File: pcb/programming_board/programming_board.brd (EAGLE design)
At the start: 57.9 x 35.5 mm, 34 parts

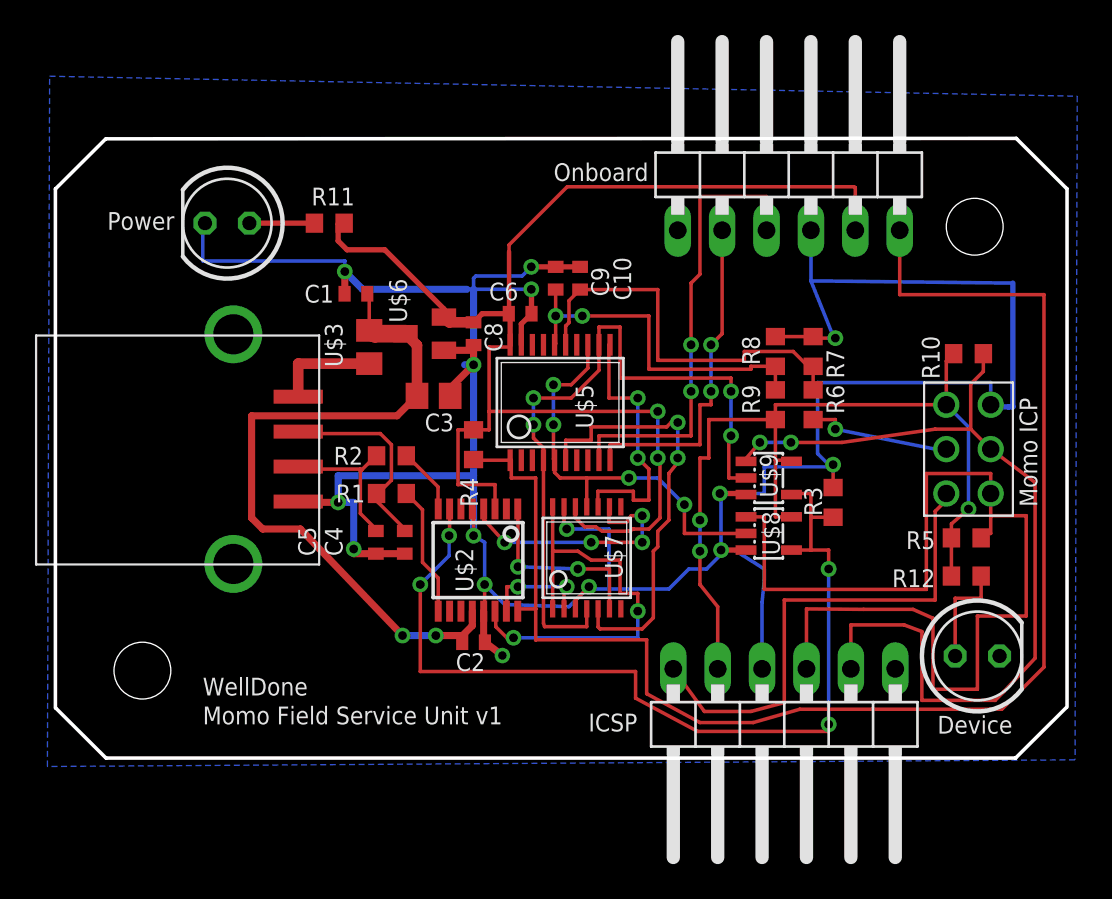
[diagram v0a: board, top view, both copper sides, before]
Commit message: Updated MoMo FSU to version 2.  Following major changes: 1. Removed unneeded header for momo programming. 2. Removed mux and analog switches allowing serial passthrough, all communication with momo will be over mib. 3. standardized momo connector 4. relaid out board
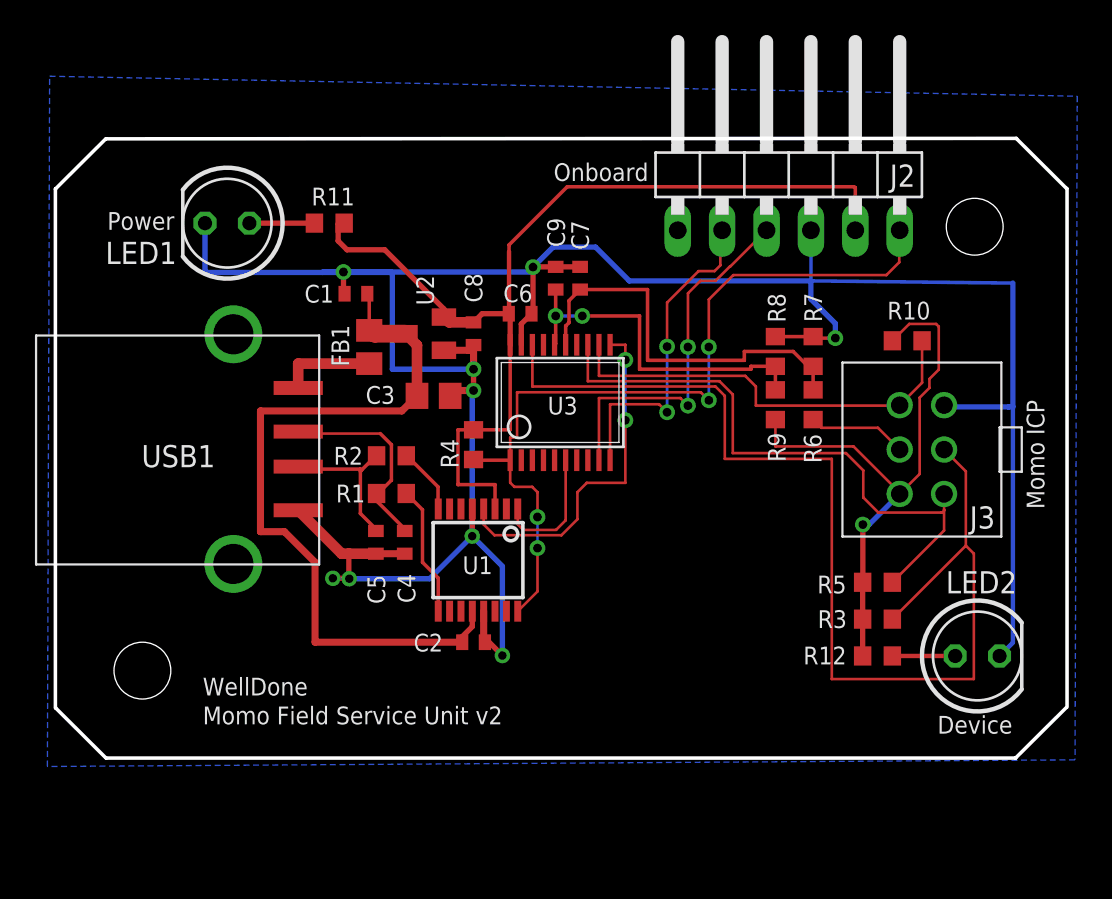
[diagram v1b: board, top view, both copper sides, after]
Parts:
- removed MOMO-ICSP: (no value), pinhead:1X06/90
- removed U$4: 2X3-MOLEX-90130, components:2X3-MOLEX-90130
- removed U$7: DG636, components:TSSOP14
- removed U$8, U$9: TS5A1066-SPST, components:SOT23-5L
- added J3: MOMO-SENSOR-HEADER, components:2X3-MOLEX-90130
- moved R3 7.15 mm to (73.7, 29.9), turned to 180 degrees
- moved R12 6.83 mm to (73.7, 27.8)
- moved R5 5.68 mm to (73.7, 32.0)
- moved R10 3.58 mm to (75.4, 45.8)
- renumbered C10 to C7, JP1 to J2, U$1 to USB1, U$2 to U1, U$3 to FB1, U$5 to U3, U$6 to U2
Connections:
- removed net DATATX: U$7.11, U$8.2, U3.13, U3.5
- removed net N$10: U$7.2, U1.15
- removed net N$11: U$7.1, U$7.14, U1.14
- removed net N$6: MOMO-ICSP.6, U$4.1
- removed net N$7: R3.2, U$8.4, U$9.4, U1.7
- removed net PGC: MOMO-ICSP.2, R10.1, U$4.5, U$9.1
- removed net PGD: MOMO-ICSP.3, R5.1, U$4.4, U$8.1
- removed net USBRX: U$7.9, U1.4
- removed net USBTX: U$7.6, U1.1
- new net ALARM: J3.5, R3.1, U3.18
- new net CLOCK: J3.3, R10.1, U3.12
- new net DATA: J3.4, R5.1, U3.13
- net +3V3: now also J3.1, R3.2; no longer MOMO-ICSP.5, U$4.3, U$8.5, U$9.5
- net CLOCKRX: no longer U$7.4, U$9.2, U3.12
- net GND: now also J3.6; no longer MOMO-ICSP.4, R3.1, U$4.6, U$7.13, U$7.3, U$8.3, U$9.3
- net PICRX1: now also U1.1; no longer U$7.5
- net PICTX1: now also U1.4; no longer U$7.10
- net V+: now also J3.2; no longer U$4.2
- net VCCIO: no longer U$7.12
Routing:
- net ALARM: track 0.00 -> 63.9 mm
- net PGD: track 61.0 -> 0.00 mm
- net N$7: track 53.7 -> 0.00 mm, vias 4 -> 0
- net PGC: track 51.1 -> 0.00 mm, vias 2 -> 0
- net CLOCKRX: track 40.9 -> 0.00 mm, vias 4 -> 0
- net DATA: track 0.00 -> 34.8 mm
- net N$21: track 82.0 -> 47.3 mm, vias 0 -> 4
- net N$6: track 28.5 -> 0.00 mm
- net N$11: track 24.6 -> 0.00 mm, vias 2 -> 0
- net CLOCK: track 0.00 -> 24.6 mm
- net DATATX: track 23.8 -> 0.00 mm, vias 4 -> 0
- net GND: track 177.7 -> 154.1 mm, vias 15 -> 9
- net VCCIO: track 79.2 -> 57.4 mm, vias 2 -> 0
- net PICRX1: track 24.6 -> 7.44 mm, vias 2 -> 0
- net +3V3: track 51.0 -> 33.8 mm, vias 3 -> 1
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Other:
- board text added: "Momo Field Service Unit v2"
- board text removed: "ICSP"
- board text removed: "Momo Field Service Unit v1"

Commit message: Update MoMo FSU with modular connector
- relay out to fix Polycase USB-31 case.
- board is finished and ready for fabrication
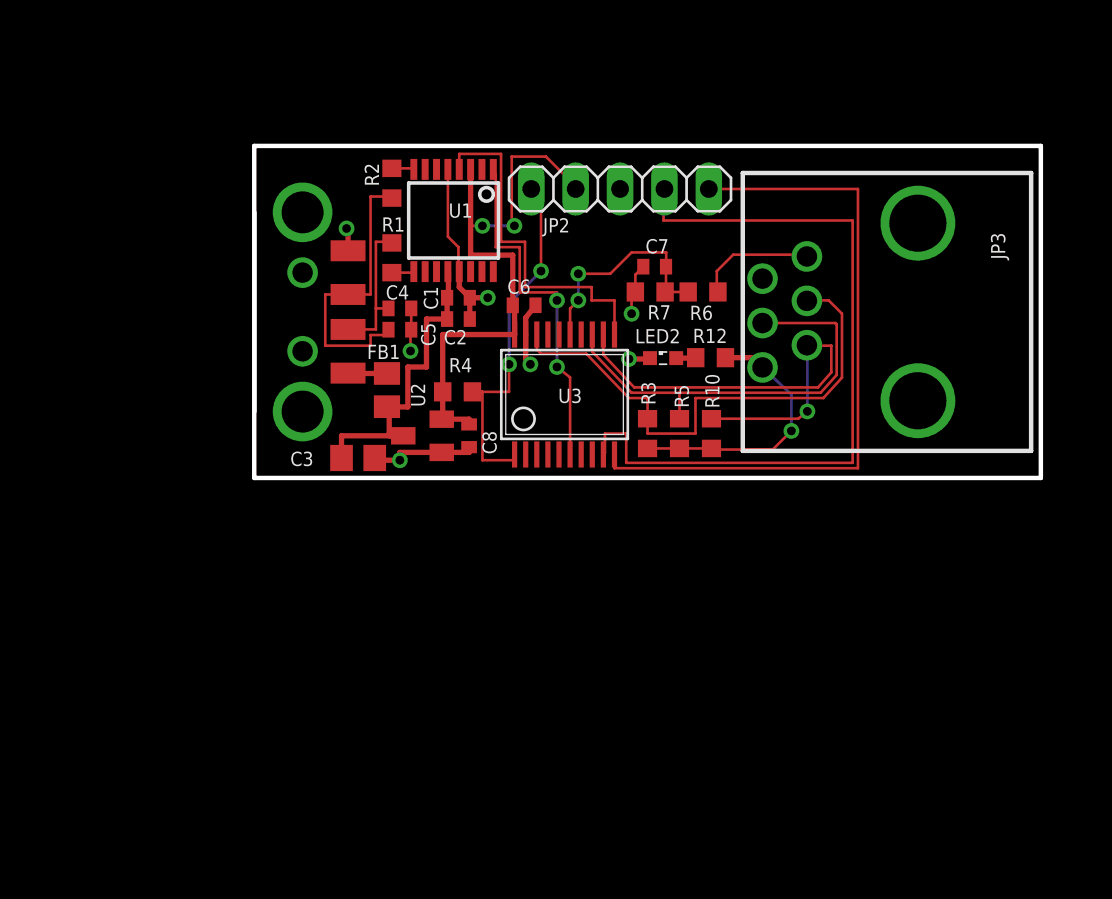
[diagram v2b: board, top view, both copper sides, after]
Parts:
- removed C9: 100 nF, rcl:C0402
- removed J2: (no value), pinhead:1X06/90
- removed J3: MOMO-SENSOR-HEADER, components:2X3-MOLEX-90130
- removed LED1: (no value), led:LED5MM
- removed R11: 66R, rcl:R0603
- removed R8: 10K, rcl:R0603
- removed R9: 1K, rcl:R0603
- removed USB1: USB-A, components:USB-A
- added JP1: MOLEX-USB-CONN, components:USB-MALE-EDGE
- added JP2: (no value), pinhead:1X05
- added JP3: MOMO-SENSOR-RJ11-VERT, components:RJ12-VERT
- LED2: device led:LED5MM -> led:SML0603
- R12: value 66R -> 68R
- moved LED2 24.8 mm to (61.4, 44.9)
- moved R12 19.6 mm to (64.1, 44.9), turned to 0 degrees
- moved U1 19.5 mm to (49.4, 52.7)
- moved C2 18.5 mm to (49.7, 47.1)
- moved R3 16.9 mm to (60.5, 40.5), turned to 270 degrees
- moved R2 15.6 mm to (45.9, 54.9), turned to 90 degrees
- moved R5 14.2 mm to (62.3, 40.5), turned to 270 degrees
- moved R1 13.5 mm to (45.9, 50.6), turned to 270 degrees
- moved C4 13.4 mm to (46.3, 47.7), turned to 0 degrees
- moved R10 12.4 mm to (64.2, 40.5), turned to 270 degrees
- moved C5 12.2 mm to (46.3, 46.5), turned to 0 degrees
- moved R7 9.92 mm to (60.7, 48.6), turned to 0 degrees
- moved R6 9.02 mm to (63.7, 48.6), turned to 0 degrees
- moved C1 5.87 mm to (49.7, 48.3), turned to 0 degrees
- moved C8 5.85 mm to (50.3, 40.4)
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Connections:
- removed net N$12: LED1.A, R11.1
- removed net N$20: C9.1, R8.2, R9.1, U3.16
- net +3V3: now also JP3.1; no longer J3.1, R9.2
- net ALARM: now also JP3.4; no longer J3.5
- net CLOCK: now also JP3.2; no longer J3.3
- net DATA: now also JP3.3; no longer J3.4
- net GND: now also JP1.4, JP2.3, JP3.5, LED2.C; no longer C9.2, J2.4, J3.6, LED1.K, LED2.K, R8.1, USB1.GND
- net N$1: now also JP1.2; no longer USB1.D-
- net N$2: now also JP1.1; no longer USB1.VBUS
- net N$21: now also JP2.5; no longer J2.6, U1.16
- net N$3: now also JP1.3; no longer USB1.D+
- net N$8: now also JP2.1; no longer J2.2
- net N$9: now also JP2.2; no longer J2.3
- net V+: now also JP3.6; no longer J3.2
- net VCCIO: now also JP2.4; no longer J2.5, R11.2
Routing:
- net GND: track 154.1 -> 28.1 mm, vias 9 -> 7
- net ALARM: track 63.9 -> 30.1 mm
- net N$21: track 47.3 -> 21.7 mm, vias 4 -> 2
- net +5V: track 43.2 -> 17.8 mm
- net VCCIO: track 57.4 -> 34.0 mm, vias 0 -> 2
- net N$9: track 21.2 -> 43.6 mm, vias 2 -> 0
- net N$20: track 20.3 -> 0.00 mm, vias 2 -> 0
- net N$8: track 18.9 -> 39.2 mm, vias 2 -> 0
- net +3V3: track 33.8 -> 16.0 mm
- net PICRX1: track 7.44 -> 20.2 mm, vias 0 -> 2
- net N$17: track 23.1 -> 12.8 mm, vias 0 -> 2
- net DATA: track 34.8 -> 25.1 mm
- net N$3: track 8.78 -> 16.9 mm
- net N$4: track 7.49 -> 1.31 mm
- net N$12: track 3.72 -> 0.00 mm
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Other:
- board size 57.9 x 35.5 mm -> 45 x 19 mm
- board text removed: "Device"
- board text removed: "Momo Field Service Unit v2"
- board text removed: "Momo ICP"
- board text removed: "Onboard"
- board text removed: "Power"
- board text removed: "WellDone"
